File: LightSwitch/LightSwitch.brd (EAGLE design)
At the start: 78.7 x 50.5 mm, 27 parts, among them Q2 TIP120, Y1 16MHz

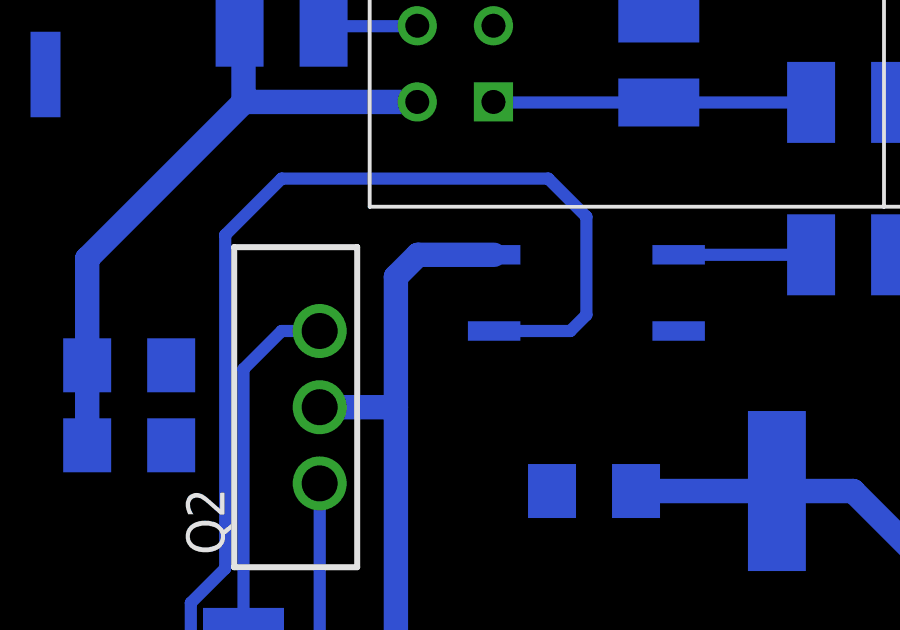
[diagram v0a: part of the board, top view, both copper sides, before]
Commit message: Fix stub wire
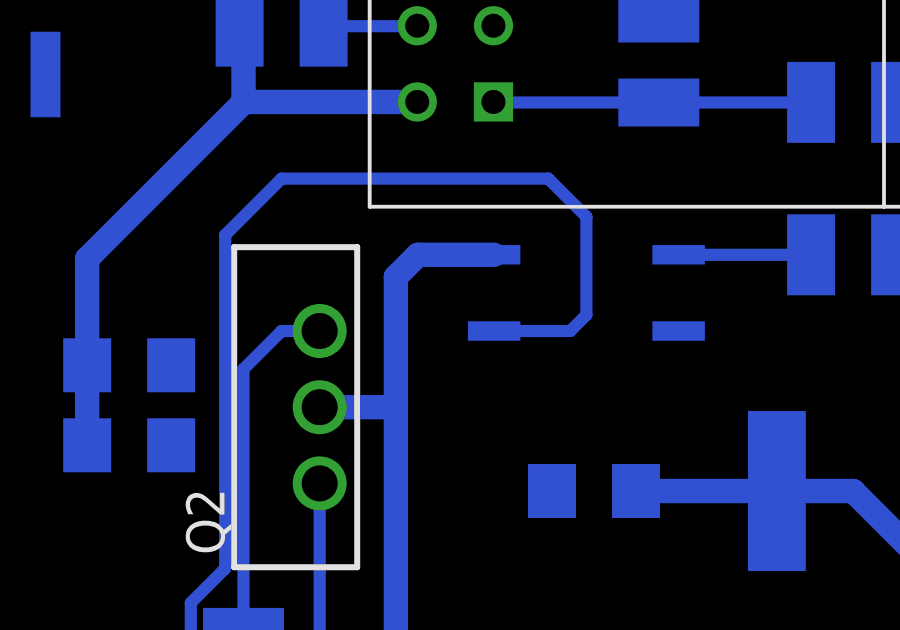
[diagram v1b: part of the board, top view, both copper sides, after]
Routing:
- net 5VCC: track 161.7 -> 161.0 mm
- net OPTO_EMITTER: track 45.1 -> 44.6 mm
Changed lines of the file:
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@@
 <wire x1="55.88" y1="20.32" x2="55.88" y2="41.91" width="0.8128" layer="16"/>
 <wire x1="55.88" y1="41.91" x2="53.34" y2="41.91" width="0.8128" layer="16"/>
-<wire x1="53.34" y1="41.91" x2="54.075" y2="41.91" width="0.8128" layer="16"/>
 <wire x1="55.88" y1="41.91" x2="55.88" y2="46.255" width="0.8128" layer="16"/>
 <wire x1="56.615" y1="46.99" x2="59.155" y2="46.99" width="0.8128" layer="16"/>
@@
 <contactref element="OPTO" pad="3"/>
 <contactref element="Q2" pad="1"/>
-<wire x1="59.155" y1="44.45" x2="59.6597375" y2="44.45" width="0.4064" layer="16"/>
-<wire x1="62.23" y1="44.985" x2="61.695" y2="44.45" width="0.4064" layer="16"/>
-<wire x1="59.155" y1="44.45" x2="61.695" y2="44.45" width="0.4064" layer="16"/>
-<wire x1="62.23" y1="44.985" x2="62.23" y2="48.26" width="0.4064" layer="16"/>
+<wire x1="62.23" y1="48.26" x2="62.23" y2="44.985" width="0.4064" layer="16"/>
 <wire x1="62.23" y1="48.26" x2="60.96" y2="49.53" width="0.4064" layer="16"/>
 <wire x1="60.96" y1="49.53" x2="52.07" y2="49.53" width="0.4064" layer="16"/>
@@
 <wire x1="53.34" y1="39.37" x2="53.34" y2="34.29" width="0.4064" layer="16"/>
 <wire x1="50.1904" y1="47.6504" x2="50.1904" y2="36.5351375" width="0.4064" layer="16"/>
+<wire x1="62.23" y1="44.985" x2="61.695" y2="44.45" width="0.4064" layer="16"/>
+<wire x1="61.695" y1="44.45" x2="59.155" y2="44.45" width="0.4064" layer="16"/>
 </signal>
 <signal name="N$4">

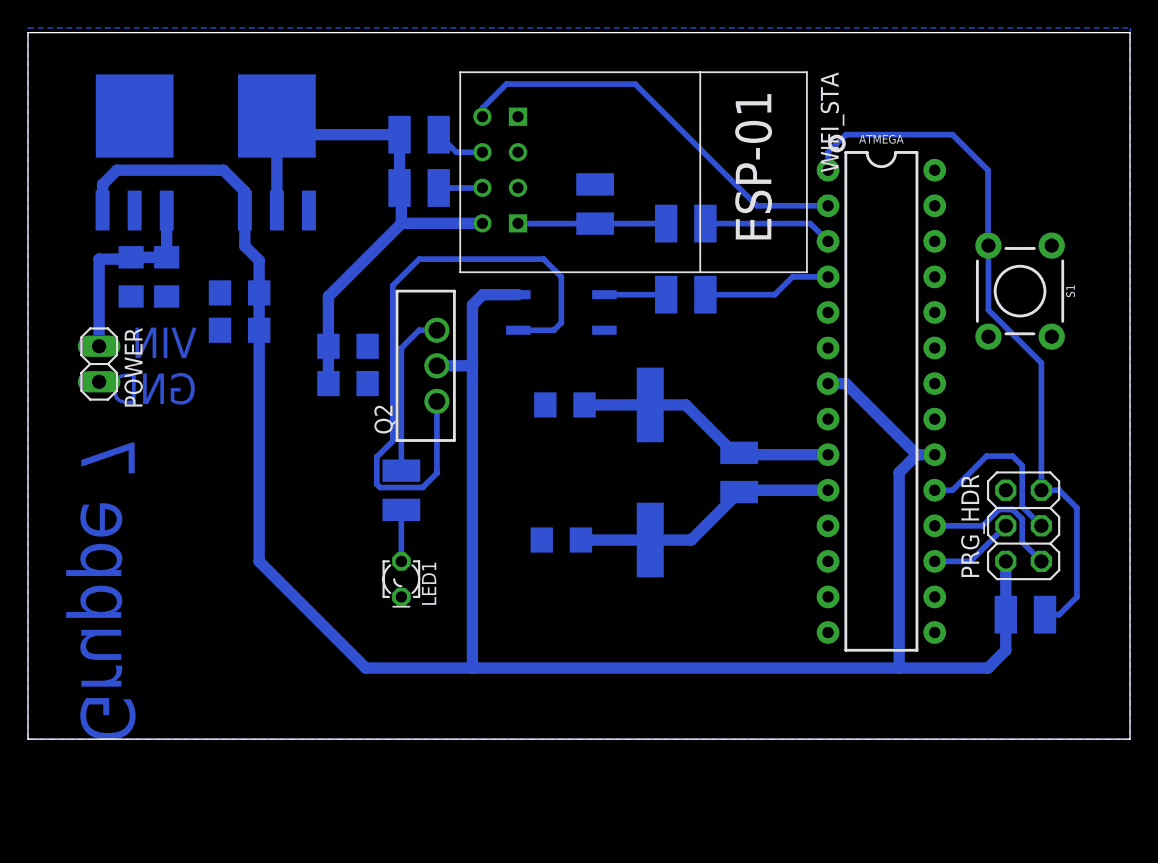
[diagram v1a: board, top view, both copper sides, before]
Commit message: Add resistors and voltage regulator as well as pinheader
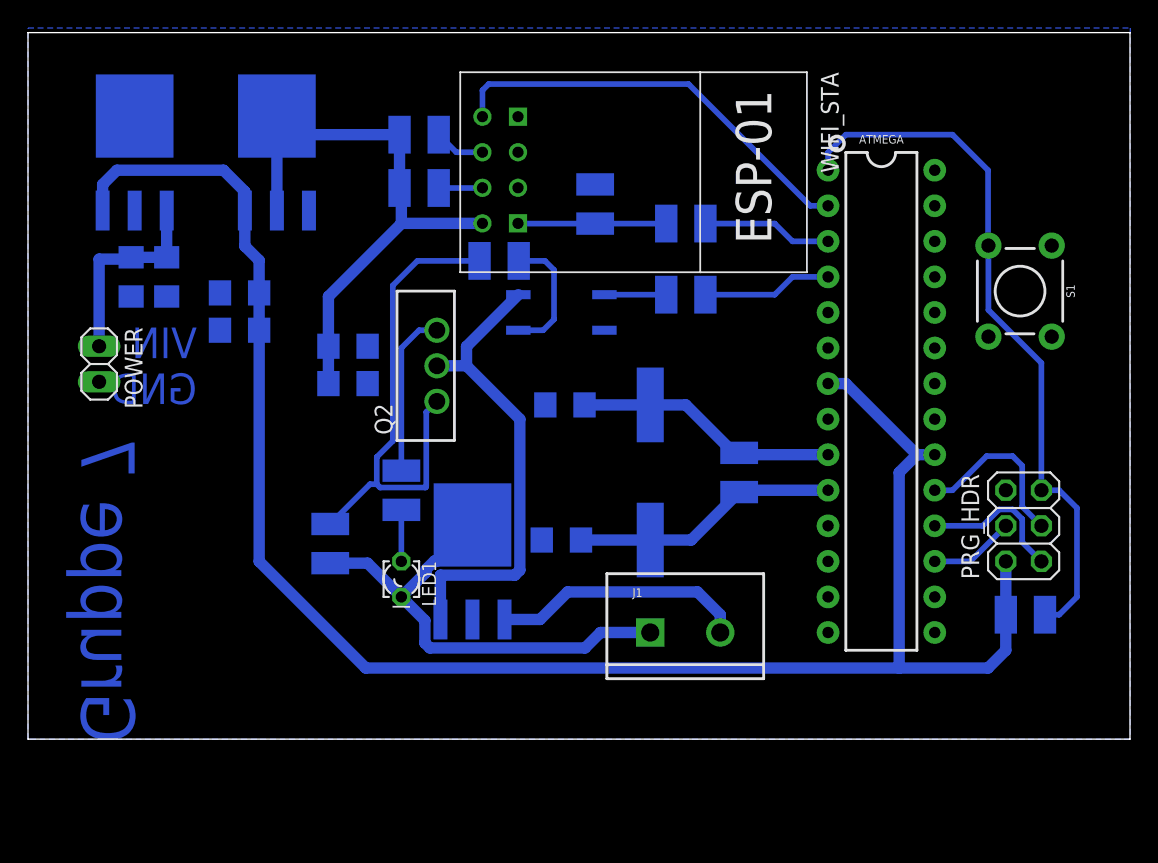
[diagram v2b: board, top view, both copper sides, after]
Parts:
- added J1: (no value), SparkFun-Connectors:SCREWTERMINAL-5MM-2
- added LED_REG: LP2950CDT-5.0G, LP2950CDT-5.0G:TO229P990X238-4N
- added R7: 3k3Ω, eagle-ltspice:R1210
- added R8: 2k2Ω, eagle-ltspice:R1210
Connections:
- new net GND_(NOPAD): LED_REG.2
- new net LED_GND: J1.1, LED1.K, LED_REG.4, R8.2
- new net LED_VCC: LED_REG.3, OPTO.4, Q2.2
- new net LED_VIN: J1.2, LED_REG.1
- new net N$1: OPTO.3, R7.2
- net 5VCC: no longer OPTO.4, Q2.2
- net GND: no longer LED1.K
- net OPTO_EMITTER: now also R7.1, R8.1; no longer OPTO.3
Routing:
- net LED_GND: track 0.00 -> 34.1 mm
- net LED_VCC: track 0.00 -> 33.9 mm
- net 5VCC: track 161.0 -> 128.9 mm
- net LED_VIN: track 0.00 -> 18.2 mm
- net N$1: track 0.00 -> 9.19 mm
- net OPTO_EMITTER: track 44.6 -> 36.2 mm
- net STA_TXD: track 29.6 -> 30.4 mm

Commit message: my name chef
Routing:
- net LED_VCC: track 33.9 -> 35.4 mm
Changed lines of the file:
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@@
 <wire x1="59.2646" y1="27.31249375" x2="58.90750625" y2="26.9554" width="0.8128" layer="16"/>
 <wire x1="55.4546" y1="41.91" x2="53.34" y2="41.91" width="0.8128" layer="16"/>
-<wire x1="59.155" y1="46.99" x2="55.4546" y2="43.2896" width="0.8128" layer="16"/>
-<wire x1="55.4546" y1="43.2896" x2="55.4546" y2="41.91" width="0.8128" layer="16"/>
+<wire x1="59.155" y1="46.99" x2="56.615" y2="46.99" width="0.8128" layer="16"/>
+<wire x1="56.615" y1="46.99" x2="55.4546" y2="45.8296" width="0.8128" layer="16"/>
+<wire x1="55.4546" y1="45.8296" x2="55.4546" y2="41.91" width="0.8128" layer="16"/>
 <wire x1="55.4546" y1="41.91" x2="59.2646" y2="38.1" width="0.8128" layer="16"/>
 <wire x1="59.2646" y1="38.1" x2="59.2646" y2="27.31249375" width="0.8128" layer="16"/>

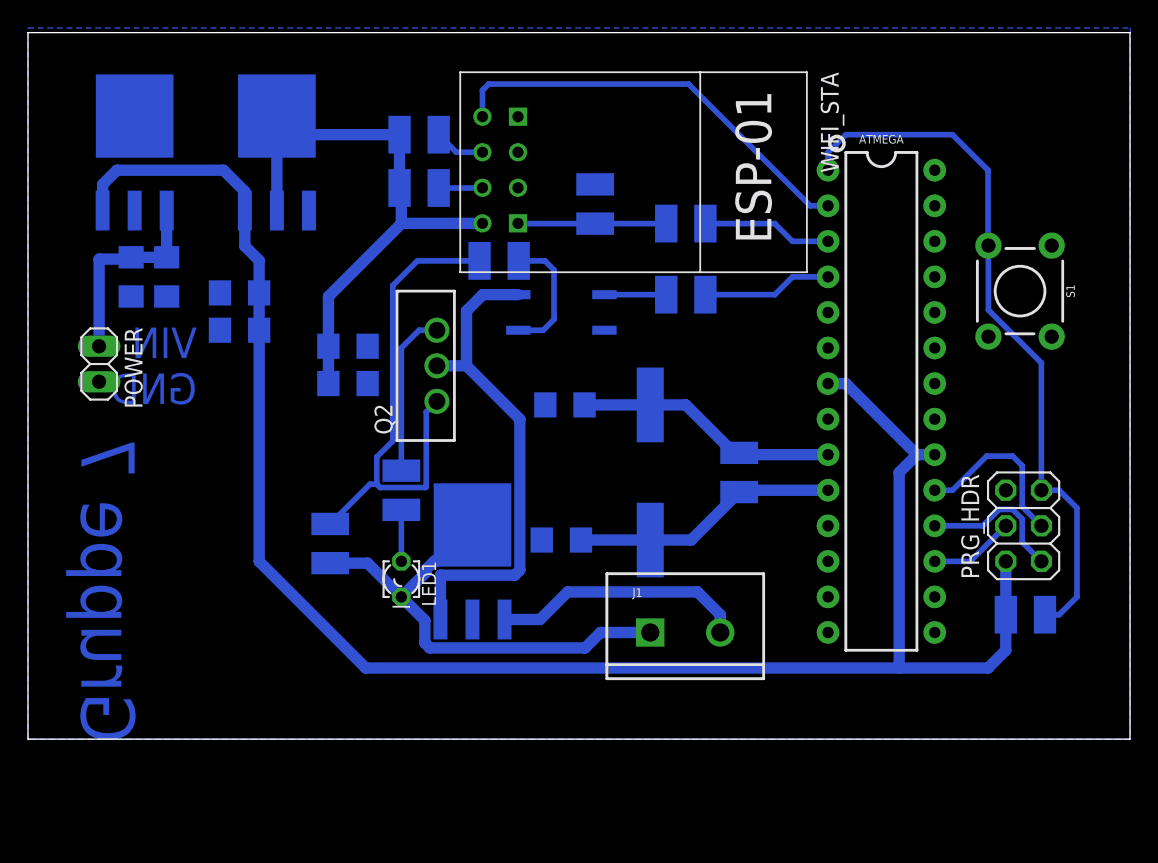
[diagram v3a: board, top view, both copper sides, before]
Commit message: Updated Boards, mainly changing up the Servomotor print due to cluttering
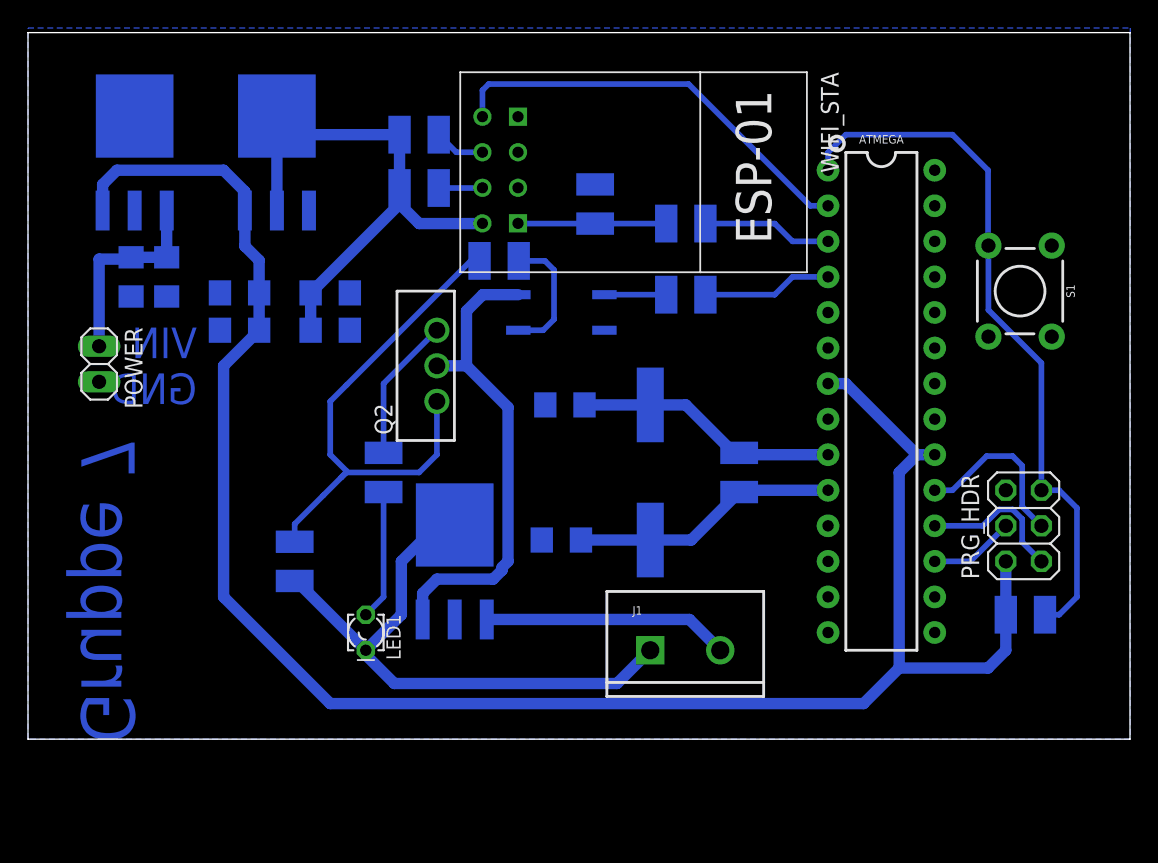
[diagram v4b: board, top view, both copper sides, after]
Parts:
- moved LED1 4.58 mm to (48.3, 22.9)
- moved C6 4.02 mm to (45.7, 44.5)
- moved C9 4.02 mm to (45.7, 47.1)
- moved R8 2.84 mm to (43.2, 27.9)
- moved R5 1.80 mm to (49.5, 34.3)
- moved LED_REG 1.27 mm to (54.6, 27.9)
- moved J1 1.27 mm to (68.6, 21.6)
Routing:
- net LED_GND: track 34.1 -> 41.9 mm
- net 5VCC: track 128.9 -> 136.1 mm
- net LED_ANODE: track 3.68 -> 9.29 mm
- net OPTO_EMITTER: track 36.2 -> 38.8 mm
- net N$4: track 11.8 -> 10.3 mm
- net 3VCC: track 41.9 -> 40.5 mm
- net LED_VCC: track 35.4 -> 34.4 mm
- net LED_VIN: track 18.2 -> 17.6 mm

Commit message: wifitracker fix
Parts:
- R7: value 3k3Ω -> 1kΩ
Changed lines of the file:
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@@
 <attribute name="VALUE" x="45.7708" y="24.13" size="1.016" layer="27" ratio="10" rot="R270"/>
 </element>
-<element name="R7" library="eagle-ltspice" library_urn="urn:adsk.eagle:library:217" package="R1210" package3d_urn="urn:adsk.eagle:package:13299/1" value="3k3Ω" x="57.785" y="49.403" smashed="yes" rot="MR180">
+<element name="R7" library="eagle-ltspice" library_urn="urn:adsk.eagle:library:217" package="R1210" package3d_urn="urn:adsk.eagle:package:13299/1" value="1kΩ" x="57.785" y="49.403" smashed="yes" rot="MR180">
 <attribute name="NAME" x="55.245" y="47.498" size="1.27" layer="26" rot="MR180"/>
 <attribute name="SPICEMODEL" value="NONE" x="57.785" y="49.403" size="1.778" layer="28" rot="MR180" display="off"/>
